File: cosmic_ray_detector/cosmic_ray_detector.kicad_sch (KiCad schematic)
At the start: 0 parts

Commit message: add title block to schematics
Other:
- company: (none) -> University of Oxford
- title: (none) -> AITL Simple Cosmic Ray Detector
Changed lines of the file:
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@@
 (kicad_sch (version 20211123) (generator eeschema)
   (paper "A4")
+  (title_block
+    (title "AITL Simple Cosmic Ray Detector")
+    (company "University of Oxford")
+    (comment 1 "design by: Dan Weatherill")
+  )
   (sheet (at 33.02 48.26) (size 69.85 34.29) (fields_autoplaced)
     (stroke (width 0.1524) (type solid) (color 0 0 0 0))

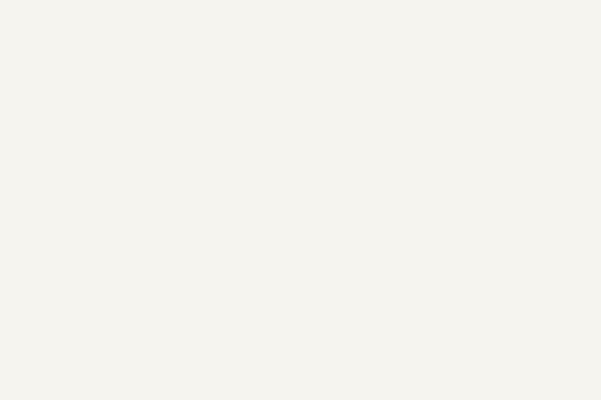
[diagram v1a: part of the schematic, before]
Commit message: draw power regulators sheet
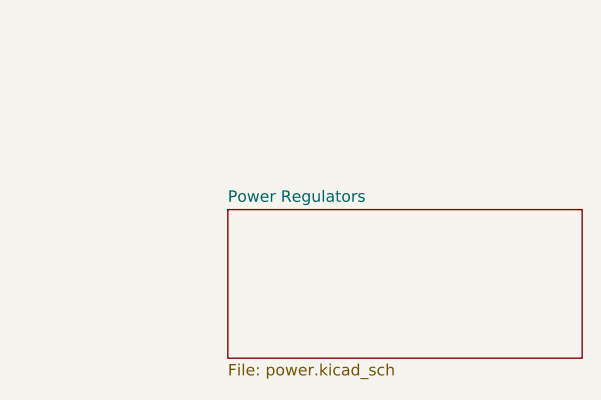
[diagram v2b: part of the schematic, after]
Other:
- added sheet Power Regulators (power.kicad_sch)
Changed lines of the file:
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@@
+    )
+  )
+  (sheet (at 170.18 83.82) (size 39.37 16.51) (fields_autoplaced)
+    (stroke (width 0.1524) (type solid) (color 0 0 0 0))
+    (fill (color 0 0 0 0.0000))
+    (property "Sheet name" "Power Regulators" (id 0) (at 170.18 83.1084 0)
+      (effects (font (size 1.27 1.27)) (justify left bottom))
+    )
+    (property "Sheet file" "power.kicad_sch" (id 1) (at 170.18 100.9146 0)
+      (effects (font (size 1.27 1.27)) (justify left top))
     )
   )
@@
     (path "/" (page "1"))
     (path "/6f9e921d-fe8f-4a5a-8c5c-cbe4afe99abc" (page "2"))
+    (path "/a7a79d2b-04f1-477d-ba1e-3ead0da72cb2" (page "3"))
   )
   (symbol_instances
@@
       (reference "#PWR?") (unit 1) (value "GNDA") (footprint "")
     )
+    (path "/a7a79d2b-04f1-477d-ba1e-3ead0da72cb2/756a1507-197a-4c44-94ef-e8e9a1eef76a"
+      (reference "#PWR?") (unit 1) (value "-5VA") (footprint "")
+    )
     (path "/6f9e921d-fe8f-4a5a-8c5c-cbe4afe99abc/7679be59-26dc-4454-b2da-eed77ae8ca61"
       (reference "#PWR?") (unit 1) (value "+5VA") (footprint "")
+    )
+    (path "/a7a79d2b-04f1-477d-ba1e-3ead0da72cb2/9655ba35-47d3-4169-b523-4be8b3cae6cb"
+      (reference "#PWR?") (unit 1) (value "GNDA") (footprint "")
     )
     (path "/6f9e921d-fe8f-4a5a-8c5c-cbe4afe99abc/bc0e4a6e-3840-474e-ac2c-78c98c270528"
@@
       (reference "#PWR?") (unit 1) (value "GNDA") (footprint "")
     )
+    (path "/a7a79d2b-04f1-477d-ba1e-3ead0da72cb2/f52ef7d1-297a-4568-9461-772fe93412e2"
+      (reference "#PWR?") (unit 1) (value "+5VA") (footprint "")
+    )
     (path "/6f9e921d-fe8f-4a5a-8c5c-cbe4afe99abc/352e1d1f-d8c0-4df3-82c0-73f9fc548b81"
       (reference "C?") (unit 1) (value "~") (footprint "")
     )
+    (path "/a7a79d2b-04f1-477d-ba1e-3ead0da72cb2/47bec3f2-2465-4aeb-9885-7c5ce317b7e4"
+      (reference "C?") (unit 1) (value "10uF") (footprint "")
+    )
+    (path "/a7a79d2b-04f1-477d-ba1e-3ead0da72cb2/4b8fbe85-76b0-4124-a5a3-59a8051e7609"
+      (reference "C?") (unit 1) (value "10nF") (footprint "")
+    )
     (path "/6f9e921d-fe8f-4a5a-8c5c-cbe4afe99abc/64d6d08c-f5e1-413e-9e3e-c0a6aeb2fc5f"
       (reference "C?") (unit 1) (value "C") (footprint "")
+    )
+    (path "/a7a79d2b-04f1-477d-ba1e-3ead0da72cb2/71923108-ae47-4f0d-8f85-d0c61523d4ff"
+      (reference "C?") (unit 1) (value "10nF") (footprint "")
+    )
+    (path "/a7a79d2b-04f1-477d-ba1e-3ead0da72cb2/79ed462d-78ce-428f-b78d-4ae19b33c4e8"
+      (reference "C?") (unit 1) (value "22nF") (footprint "")
     )
     (path "/6f9e921d-fe8f-4a5a-8c5c-cbe4afe99abc/9342db19-454a-448f-a9b0-e083f29fdbc6"
@@
     (path "/6f9e921d-fe8f-4a5a-8c5c-cbe4afe99abc/ade73c7f-6d57-424e-b3c9-b2d23c54b285"
       (reference "C?") (unit 1) (value "~") (footprint "")
+    )
+    (path "/a7a79d2b-04f1-477d-ba1e-3ead0da72cb2/b0a82baf-ff23-42e4-95ab-ccde60e13fd7"
+      (reference "C?") (unit 1) (value "10uF") (footprint "")
+    )
+    (path "/a7a79d2b-04f1-477d-ba1e-3ead0da72cb2/b873aaae-3580-4bc9-8b5a-0df5ac47c43f"
+      (reference "C?") (unit 1) (value "22nF") (footprint "")
     )
     (path "/6f9e921d-fe8f-4a5a-8c5c-cbe4afe99abc/b8ce0ab1-12e9-4729-8cf0-b6c9aa72ce7b"
@@
       (reference "C?") (unit 1) (value "~") (footprint "")
     )
+    (path "/a7a79d2b-04f1-477d-ba1e-3ead0da72cb2/d84d3b19-8918-4b4c-899a-aa4a8a4bb9b5"
+      (reference "C?") (unit 1) (value "10nF") (footprint "")
+    )
+    (path "/a7a79d2b-04f1-477d-ba1e-3ead0da72cb2/e70e6158-5df2-4b28-bcf8-431998879b2d"
+      (reference "C?") (unit 1) (value "10uF") (footprint "")
+    )
     (path "/6f9e921d-fe8f-4a5a-8c5c-cbe4afe99abc/5ce095f3-e38c-45ce-8672-a4bac6e6c0b6"
       (reference "D?") (unit 1) (value "VBPW34FAS") (footprint "VBPW34FAS")
+    )
+    (path "/a7a79d2b-04f1-477d-ba1e-3ead0da72cb2/9bea8bdd-b087-4fac-a78f-b3ebb429045e"
+      (reference "D?") (unit 1) (value "12V") (footprint "Diode_SMD:D_SOD-123")
+    )
+    (path "/a7a79d2b-04f1-477d-ba1e-3ead0da72cb2/cb83f0da-b61c-410a-ade6-20d9d6cfa25e"
+      (reference "D?") (unit 1) (value "12V") (footprint "Diode_SMD:D_SOD-123")
+    )
+    (path "/a7a79d2b-04f1-477d-ba1e-3ead0da72cb2/2a7929ff-9f40-4bd1-bcfb-e606c3c4db50"
+      (reference "R?") (unit 1) (value "10k") (footprint "")
     )
     (path "/6f9e921d-fe8f-4a5a-8c5c-cbe4afe99abc/33970c63-f931-486c-9740-29ed26af6d58"
       (reference "R?") (unit 1) (value "~") (footprint "")
     )
+    (path "/a7a79d2b-04f1-477d-ba1e-3ead0da72cb2/355eb33b-a5b9-4f3d-ac06-a25dd984ce3d"
+      (reference "R?") (unit 1) (value "12.7k") (footprint "")
+    )
     (path "/6f9e921d-fe8f-4a5a-8c5c-cbe4afe99abc/43a8e6ec-b394-4d3f-8cb4-c9eccd98a185"
       (reference "R?") (unit 1) (value "R_US") (footprint "")
+    )
+    (path "/a7a79d2b-04f1-477d-ba1e-3ead0da72cb2/53e58d3c-d339-4677-acde-ecac96daf7c3"
+      (reference "R?") (unit 1) (value "13k") (footprint "")
+    )
+    (path "/a7a79d2b-04f1-477d-ba1e-3ead0da72cb2/59fbb484-d156-47af-8542-9f0fbf50742e"
+      (reference "R?") (unit 1) (value "10k") (footprint "")
     )
     (path "/6f9e921d-fe8f-4a5a-8c5c-cbe4afe99abc/9b646f2f-527d-40aa-802c-6f5e73d270f5"
       (reference "R?") (unit 1) (value "~") (footprint "")
     )
+    (path "/a7a79d2b-04f1-477d-ba1e-3ead0da72cb2/afc5c3f9-3c42-4bce-8ae8-32d1ae268c1e"
+      (reference "U?") (unit 1) (value "TPS7A30") (footprint "SPIRIT:MSOP-8-1EP_3x3mm_P0.65mm_EP1.73x1.85mm_ThermalVias")
+    )
+    (path "/a7a79d2b-04f1-477d-ba1e-3ead0da72cb2/b2403965-d978-49c7-a324-3bd38b59deb0"
+      (reference "U?") (unit 1) (value "TPS7A49") (footprint "SPIRIT:MSOP-8-1EP_3x3mm_P0.65mm_EP1.73x1.85mm_ThermalVias")
+    )
     (path "/6f9e921d-fe8f-4a5a-8c5c-cbe4afe99abc/dc6a577a-adb1-40f6-969b-35ca6dfaa8da"

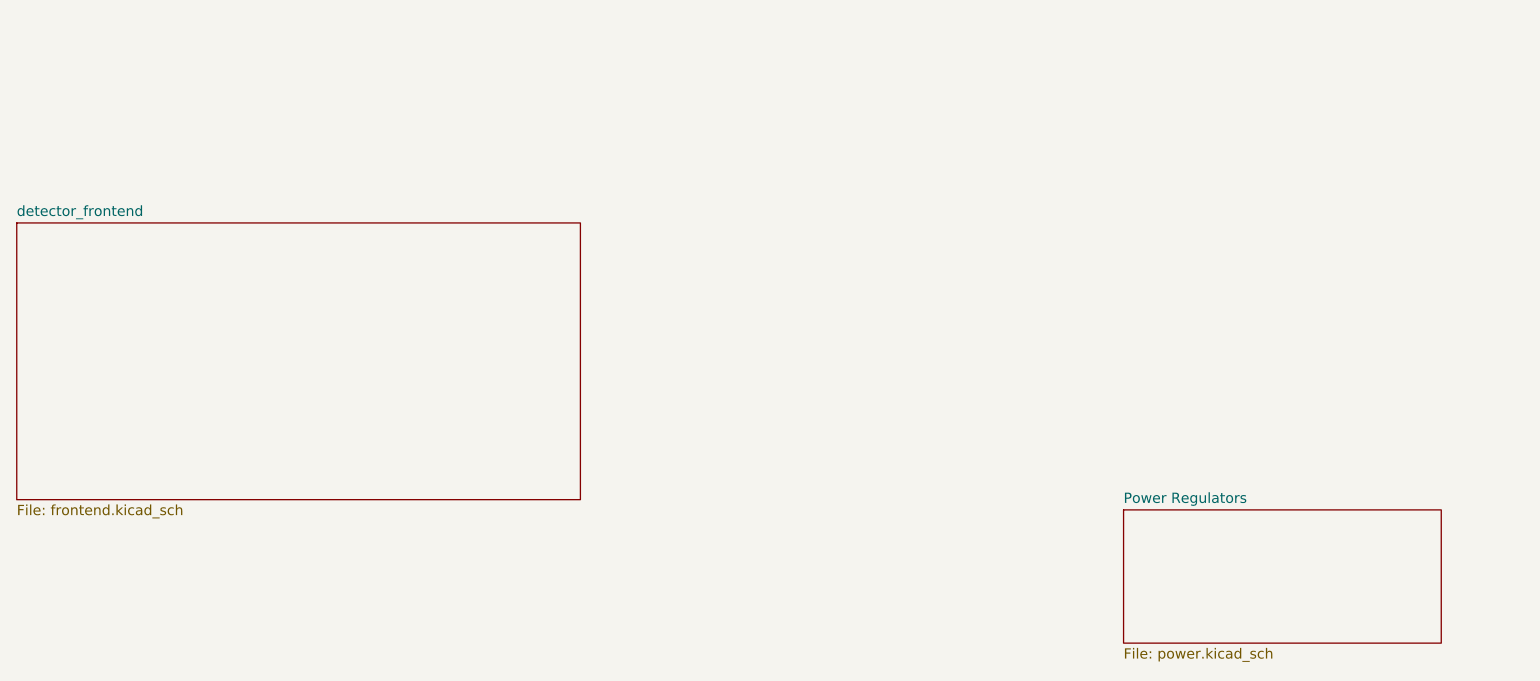
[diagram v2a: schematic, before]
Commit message: design of TLV3501 comparator sheet
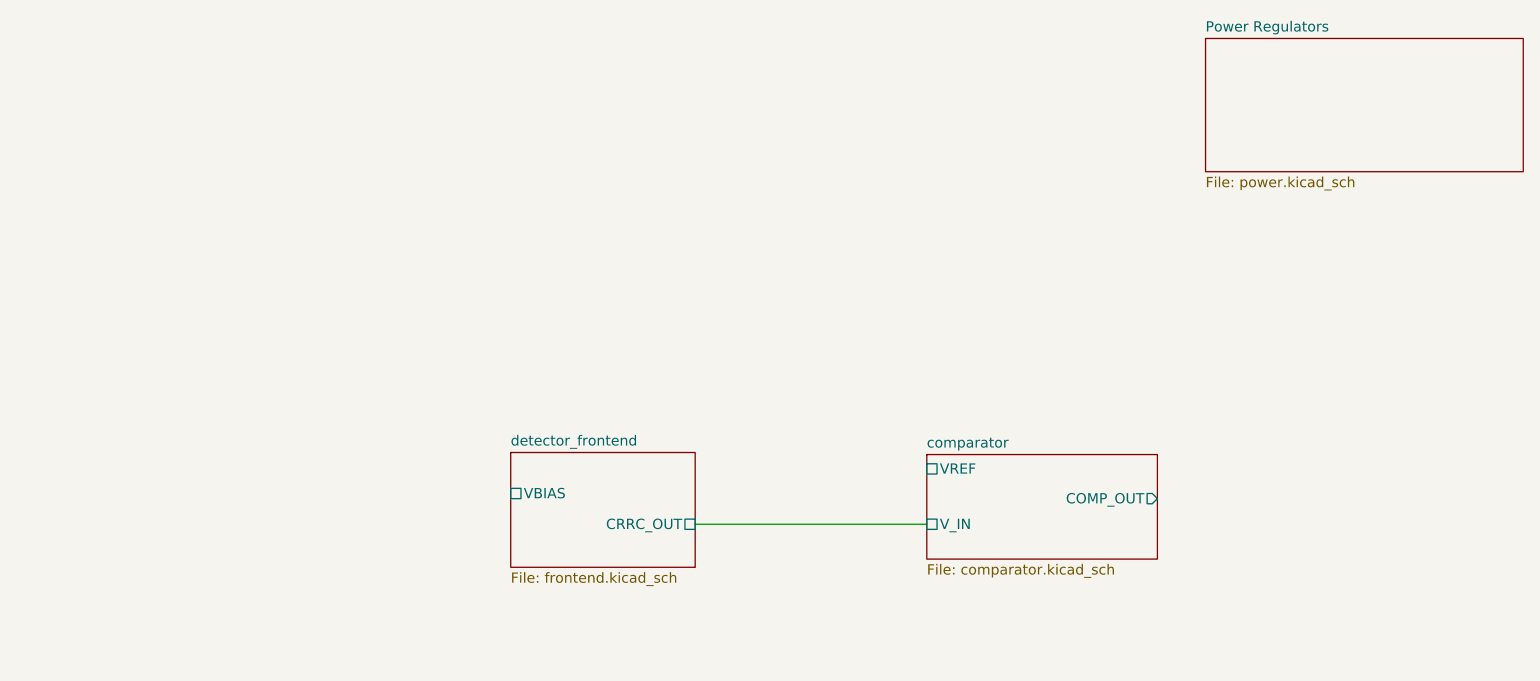
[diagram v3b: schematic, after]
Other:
- added sheet comparator (comparator.kicad_sch)
- sheet detector_frontend ports: added CRRC_OUT, VBIAS; removed none
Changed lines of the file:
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@@
     (comment 1 "design by: Dan Weatherill")
   )
-  (sheet (at 33.02 48.26) (size 69.85 34.29) (fields_autoplaced)
+  (wire (pts (xy 117.094 85.598) (xy 145.796 85.598))
+    (stroke (width 0) (type default) (color 0 0 0 0))
+  )
+  (sheet (at 94.234 76.708) (size 22.86 14.224) (fields_autoplaced)
     (stroke (width 0.1524) (type solid) (color 0 0 0 0))
     (fill (color 0 0 0 0.0000))
-    (property "Sheet name" "detector_frontend" (id 0) (at 33.02 47.5484 0)
+    (property "Sheet name" "detector_frontend" (id 0) (at 94.234 75.9964 0)
       (effects (font (size 1.27 1.27)) (justify left bottom))
     )
-    (property "Sheet file" "frontend.kicad_sch" (id 1) (at 33.02 83.1346 0)
+    (property "Sheet file" "frontend.kicad_sch" (id 1) (at 94.234 91.5166 0)
       (effects (font (size 1.27 1.27)) (justify left top))
     )
+    (pin "VBIAS" passive (at 94.234 81.788 180)
+      (effects (font (size 1.27 1.27)) (justify left))
+    )
+    (pin "CRRC_OUT" passive (at 117.094 85.598 0)
+      (effects (font (size 1.27 1.27)) (justify right))
+    )
   )
-  (sheet (at 170.18 83.82) (size 39.37 16.51) (fields_autoplaced)
+  (sheet (at 145.796 76.962) (size 28.575 12.954) (fields_autoplaced)
     (stroke (width 0.1524) (type solid) (color 0 0 0 0))
     (fill (color 0 0 0 0.0000))
-    (property "Sheet name" "Power Regulators" (id 0) (at 170.18 83.1084 0)
+    (property "Sheet name" "comparator" (id 0) (at 145.796 76.2504 0)
       (effects (font (size 1.27 1.27)) (justify left bottom))
     )
-    (property "Sheet file" "power.kicad_sch" (id 1) (at 170.18 100.9146 0)
+    (property "Sheet file" "comparator.kicad_sch" (id 1) (at 145.796 90.5006 0)
+      (effects (font (size 1.27 1.27)) (justify left top))
+    )
+    (pin "V_IN" passive (at 145.796 85.598 180)
+      (effects (font (size 1.27 1.27)) (justify left))
+    )
+    (pin "VREF" passive (at 145.796 78.74 180)
+      (effects (font (size 1.27 1.27)) (justify left))
+    )
+    (pin "COMP_OUT" output (at 174.371 82.423 0)
+      (effects (font (size 1.27 1.27)) (justify right))
+    )
+  )
+  (sheet (at 180.34 25.4) (size 39.37 16.51) (fields_autoplaced)
+    (stroke (width 0.1524) (type solid) (color 0 0 0 0))
+    (fill (color 0 0 0 0.0000))
+    (property "Sheet name" "Power Regulators" (id 0) (at 180.34 24.6884 0)
+      (effects (font (size 1.27 1.27)) (justify left bottom))
+    )
+    (property "Sheet file" "power.kicad_sch" (id 1) (at 180.34 42.4946 0)
       (effects (font (size 1.27 1.27)) (justify left top))
     )
@@
     (path "/6f9e921d-fe8f-4a5a-8c5c-cbe4afe99abc" (page "2"))
     (path "/a7a79d2b-04f1-477d-ba1e-3ead0da72cb2" (page "3"))
+    (path "/86d8b01b-5c34-47c3-904c-67d3d9a70426" (page "4"))
   )
   (symbol_instances
     (path "/6f9e921d-fe8f-4a5a-8c5c-cbe4afe99abc/0f59a441-aac2-4098-8d00-e38010974acc"
       (reference "#PWR?") (unit 1) (value "-5VA") (footprint "")
+    )
+    (path "/86d8b01b-5c34-47c3-904c-67d3d9a70426/1aa1157d-4bd6-4969-b9fb-c0b119211af2"
+      (reference "#PWR?") (unit 1) (value "+5VA") (footprint "")
     )
     (path "/6f9e921d-fe8f-4a5a-8c5c-cbe4afe99abc/57b1cafd-58e2-47d3-b840-730523ad81f3"
@@
       (reference "#PWR?") (unit 1) (value "GNDA") (footprint "")
     )
+    (path "/86d8b01b-5c34-47c3-904c-67d3d9a70426/cea002a4-2d4e-4eb1-abfb-142158fc8b9d"
+      (reference "#PWR?") (unit 1) (value "GNDA") (footprint "")
+    )
+    (path "/86d8b01b-5c34-47c3-904c-67d3d9a70426/d2c48699-040d-4a21-a5e0-4cf96efacb51"
+      (reference "#PWR?") (unit 1) (value "GNDA") (footprint "")
+    )
     (path "/a7a79d2b-04f1-477d-ba1e-3ead0da72cb2/f52ef7d1-297a-4568-9461-772fe93412e2"
       (reference "#PWR?") (unit 1) (value "+5VA") (footprint "")
     )
+    (path "/86d8b01b-5c34-47c3-904c-67d3d9a70426/1c1e93c8-4588-40f4-bfc3-97272164156b"
+      (reference "C?") (unit 1) (value "2.2uF") (footprint "")
+    )
     (path "/6f9e921d-fe8f-4a5a-8c5c-cbe4afe99abc/352e1d1f-d8c0-4df3-82c0-73f9fc548b81"
       (reference "C?") (unit 1) (value "~") (footprint "")
+    )
+    (path "/86d8b01b-5c34-47c3-904c-67d3d9a70426/36f0c0d0-5fbc-41c5-b480-ee52e9c49a15"
+      (reference "C?") (unit 1) (value "0.1uF") (footprint "")
     )
     (path "/a7a79d2b-04f1-477d-ba1e-3ead0da72cb2/47bec3f2-2465-4aeb-9885-7c5ce317b7e4"
@@
       (reference "D?") (unit 1) (value "12V") (footprint "Diode_SMD:D_SOD-123")
     )
+    (path "/86d8b01b-5c34-47c3-904c-67d3d9a70426/af3aa5f2-62c8-4412-beae-b6c8e5ade3ec"
+      (reference "IC?") (unit 1) (value "TLV3501AIDBVTG4") (footprint "SOT95P280X145-6N")
+    )
     (path "/a7a79d2b-04f1-477d-ba1e-3ead0da72cb2/2a7929ff-9f40-4bd1-bcfb-e606c3c4db50"
       (reference "R?") (unit 1) (value "10k") (footprint "")
@@
     (path "/a7a79d2b-04f1-477d-ba1e-3ead0da72cb2/355eb33b-a5b9-4f3d-ac06-a25dd984ce3d"
       (reference "R?") (unit 1) (value "12.7k") (footprint "")
+    )
+    (path "/86d8b01b-5c34-47c3-904c-67d3d9a70426/360a8f93-7c90-432a-b456-b7959e8c8583"
+      (reference "R?") (unit 1) (value "~") (footprint "")
     )
     (path "/6f9e921d-fe8f-4a5a-8c5c-cbe4afe99abc/43a8e6ec-b394-4d3f-8cb4-c9eccd98a185"
@@
       (reference "R?") (unit 1) (value "10k") (footprint "")
     )
+    (path "/86d8b01b-5c34-47c3-904c-67d3d9a70426/61b42055-9297-49b1-ae5e-21451e411d29"
+      (reference "R?") (unit 1) (value "R_US") (footprint "")
+    )
     (path "/6f9e921d-fe8f-4a5a-8c5c-cbe4afe99abc/9b646f2f-527d-40aa-802c-6f5e73d270f5"
